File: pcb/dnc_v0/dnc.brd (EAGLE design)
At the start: 100 x 80 mm, 69 parts, among them IC1 74HC595D, IC2 74HC595D, Q1 200mA/50V, Q2 TSM2306CX, Q3 TSM2306CX, Q4 TSM2306CX, Q5 TSM2306CX, Q6 200mA/50V, Q7 TSM2306CX, Q8 TSM2306CX

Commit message: First try of routing, no analog atmega ?
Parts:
- removed IC1, IC2: 74HC595D, 74xx-eu:SO16
- removed JP1, JP10, JP11, JP9: M025MM, SparkFun-Connectors:SCREWTERMINAL-5MM-2
- removed JP12, JP20, JP21: M02LOCK_LONGPADS, SparkFun-Connectors:1X02_LOCK_LONGPADS
- removed JP2, JP3, JP4: (no value), SparkFun:1X03_LOCK_LONGPADS
- removed JP22: (no value), SparkFun:1X02_LONGPADS
- removed JP5, JP6, JP7, JP8: (no value), SparkFun:1X02_LOCK_LONGPADS
- removed Q1, Q6: 200mA/50V, SparkFun-DiscreteSemi:SOT23-3
- removed Q2, Q3, Q4: TSM2306CX, SparkFun-DiscreteSemi:SOT323
- removed SV1, SV2: (no value), con-lstb:MA08-2
- removed U$1, U$2, U$3, U$6, U$7, U$8: EXT-DNC, pierre_vv:EXTPINDNC
- added 3.3/5: (no value), SparkFun:1X02_LONGPADS
- added A+_UART, IN1, IN2, IN3, IN4: (no value), SparkFun:1X02_LOCK_LONGPADS
- added A_IN1, A_IN2, A_IN3: (no value), SparkFun:1X03_LOCK_LONGPADS
- added EXT1, EXT2, EXT3, EXT4, EXT5, EXT6: EXT-DNC, pierre_vv:EXTPINDNC
- added JP_OUT1, JP_OUT2, JP_OUT3: M02LOCK_LONGPADS, SparkFun-Connectors:1X02_LOCK_LONGPADS
- added MOS_BAT, MOS_TEMP: 200mA/50V, SparkFun-DiscreteSemi:SOT23-3
- added MOS_PWR1, MOS_PWR2, MOS_PWR3: TSM2306CX, SparkFun-DiscreteSemi:SOT323
- added PWR_OUT1, PWR_OUT2, PWR_OUT3, RAW_IN: M025MM, SparkFun-Connectors:SCREWTERMINAL-5MM-2
- added REG1, REG2: 74HC595D, 74xx-eu:SO16
- added TITREUR1, TITREUR2: (no value), con-lstb:MA08-2
- moved JP14 243.8 mm to (97.8, 22.9)
- moved JP13 242.6 mm to (101.6, 25.4)
- moved Q8 205.7 mm to (83.8, 52.1)
- moved Q7 194.1 mm to (83.8, 69.8)
- moved Q5 192.8 mm to (83.8, 61.0)
- moved C2 190.4 mm to (59.7, 48.3), turned to 270 degrees
- moved RIN4 185.1 mm to (45.7, 8.89)
- moved RIN7 184.6 mm to (81.3, 12.1)
- moved RIN3 178.4 mm to (39.4, 8.89), turned to 180 degrees
- moved RIN2 172.0 mm to (33.0, 8.89)
- moved RIN6 171.6 mm to (82.5, 27.9)
- moved RIN10 170.5 mm to (82.5, 48.3)
- moved JP19 169.1 mm to (97.8, 19.1)
- moved RIN1 165.2 mm to (25.4, 8.89), turned to 180 degrees
- moved RIN5 161.0 mm to (82.5, 39.4)
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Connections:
- removed net 3.3: U$1.3.3, U$2.3.3, U$3.3.3, U$6.3.3, U$7.3.3, U$8.3.3
- removed net N$31: U$4.8
- removed net N$32: U$4.10
- removed net N$33: U$4.12
- removed net N$34: U$4.16
- new net RXA+: A+_UART.2, U$4.10
- new net TXA+: A+_UART.1, U$4.8
- net +3V3: now also 3.3/5.1, A_IN1.2, A_IN2.2, A_IN3.2, EXT1.3.3V, EXT2.3.3V, EXT3.3.3V, EXT4.3.3V, EXT5.3.3V, EXT6.3.3V, IN1.1, IN2.1, IN3.1, IN4.1, REG1.10, REG2.10; no longer IC1.10, IC2.10, JP2.2, JP22.1, JP3.2, JP4.2, JP5.1, JP6.1, JP7.1, JP8.1
- net +5V: now also 3.3/5.2, EXT1.5V, EXT2.5V, EXT3.5V, EXT4.5V, EXT5.5V, EXT6.5V, TITREUR1.12, TITREUR1.14, TITREUR1.16, TITREUR2.12, TITREUR2.14, TITREUR2.16; no longer JP22.2, Q2.3, Q3.3, Q4.3, SV1.12, SV1.14, SV1.16, SV2.12, SV2.14, SV2.16
- net /CS_EXT_1: now also EXT1./RESET; no longer U$3./RESET
- net /CS_EXT_2: now also EXT2./RESET; no longer U$1./RESET
- net /CS_EXT_3: now also EXT3./RESET; no longer U$2./RESET
- net /CS_EXT_4: now also EXT4./RESET; no longer U$6./RESET
- net /CS_EXT_5: now also EXT5./RESET; no longer U$7./RESET
- net /CS_EXT_6: now also EXT6./RESET; no longer U$8./RESET
- net ACTIVE_ANALOG_RAW: now also MOS_BAT.1; no longer Q1.1
- net ACTIVE_ANALOG_TEMP: now also MOS_TEMP.1; no longer Q6.1
- net ACTIVE_OUT_POWER_1: now also MOS_PWR1.1; no longer Q3.1, U$4.36
- net ACTIVE_OUT_POWER_2: now also MOS_PWR2.1; no longer Q2.1, U$4.38
- net ACTIVE_OUT_POWER_3: now also MOS_PWR3.1; no longer Q4.1, U$4.40
- net ANALOG_IN_1: now also A_IN1.3; no longer JP2.3
- net ANALOG_IN_2: now also A_IN2.3; no longer JP3.3
- net ANALOG_IN_3: now also A_IN3.3; no longer JP4.3
- net ANALOG_RAW: now also MOS_BAT.2; no longer Q1.2
- net ANALOG_TEMP: now also MOS_TEMP.2; no longer Q6.2
- net CODE: now also EXT1.RETOURANALOG, EXT2.RETOURANALOG, EXT3.RETOURANALOG, EXT4.RETOURANALOG, EXT5.RETOURANALOG, EXT6.RETOURANALOG; no longer U$1.RETOURANALOG, U$2.RETOURANALOG, U$3.RETOURANALOG, U$6.RETOURANALOG, U$7.RETOURANALOG, U$8.RETOURANALOG
- net GND: now also A_IN1.1, A_IN2.1, A_IN3.1, EXT1.1_GND, EXT2.1_GND, EXT3.1_GND, EXT4.1_GND, EXT5.1_GND, EXT6.1_GND, JP_OUT1.2, JP_OUT2.2, JP_OUT3.2, PWR_OUT1.2, PWR_OUT2.2, PWR_OUT3.2, RAW_IN.2, REG1.13, REG1.8, REG2.13, REG2.8, TITREUR1.11, TITREUR1.13, TITREUR1.15, TITREUR1.8, TITREUR2.11, TITREUR2.13, TITREUR2.15, TITREUR2.8; no longer IC1.13, IC1.8, IC2.13, IC2.8, JP1.2, JP10.2, JP11.2, JP12.2, JP2.1, JP20.2, JP21.2, JP3.1, JP4.1, JP9.2, SV1.11, SV1.13, SV1.15, SV1.8, SV2.11, SV2.13, SV2.15, SV2.8, U$1.1_GND, U$2.1_GND, U$3.1_GND, U$6.1_GND, U$7.1_GND, U$8.1_GND
- net IN_1: now also IN1.2; no longer JP5.2
- net IN_2: now also IN2.2; no longer JP6.2
- net IN_3: now also IN3.2; no longer JP7.2
- net IN_4: now also IN4.2; no longer JP8.2
- net MISO: now also EXT1.MISO, EXT2.MISO, EXT3.MISO, EXT4.MISO, EXT5.MISO, EXT6.MISO; no longer U$1.MISO, U$2.MISO, U$3.MISO, U$6.MISO, U$7.MISO, U$8.MISO
- net MOSI: now also EXT1.MOSI, EXT2.MOSI, EXT3.MOSI, EXT4.MOSI, EXT5.MOSI, EXT6.MOSI; no longer U$1.MOSI, U$2.MOSI, U$3.MOSI, U$6.MOSI, U$7.MOSI, U$8.MOSI
- net N$10: now also EXT6.FREE; no longer U$8.FREE
- net N$11: now also MOS_TEMP.3; no longer Q6.3
- net N$12: now also RAW_IN.1; no longer JP1.1
- net N$21: now also EXT1.FREE; no longer U$3.FREE
- net N$3: now also MOS_BAT.3; no longer Q1.3
- net N$4: now also EXT2.FREE; no longer U$1.FREE
- net N$5: now also EXT3.FREE; no longer U$2.FREE
- net N$7: now also REG1.9, REG2.14; no longer IC1.9, IC2.14
- net N$8: now also EXT4.FREE; no longer U$6.FREE
- net N$9: now also EXT5.FREE; no longer U$7.FREE
- net OUT_1: now also JP_OUT1.1; no longer JP12.1
- net OUT_2: now also JP_OUT2.1; no longer JP20.1
- net OUT_3: now also JP_OUT3.1; no longer JP21.1
- net OUT_POWER_1: now also MOS_PWR1.2, PWR_OUT1.1; no longer JP9.1, Q3.2
- net OUT_POWER_2: now also MOS_PWR2.2, PWR_OUT2.1; no longer JP10.1, Q2.2
- net OUT_POWER_3: now also MOS_PWR3.2, PWR_OUT3.1; no longer JP11.1, Q4.2
- net RAW: now also EXT1.RAW, EXT2.RAW, EXT3.RAW, EXT4.RAW, EXT5.RAW, EXT6.RAW, MOS_PWR1.3, MOS_PWR2.3, MOS_PWR3.3; no longer U$1.RAW, U$2.RAW, U$3.RAW, U$6.RAW, U$7.RAW, U$8.RAW
- net RD: now also TITREUR1.6, TITREUR2.6; no longer SV1.6, SV2.6
- net REG_RCK: now also REG1.12, REG2.12; no longer IC1.12, IC2.12
- net REG_SCK: now also REG1.11, REG2.11; no longer IC1.11, IC2.11
- net REG_VAL: now also REG1.14; no longer IC1.14
- net RST1: now also REG1.15, TITREUR1.1; no longer IC1.15, SV1.1
- net RST10: now also REG2.1; no longer IC2.1
- net RST11: now also REG2.2; no longer IC2.2
- net RST12: now also REG2.3; no longer IC2.3
- net RST13: now also REG2.4; no longer IC2.4
- net RST14: now also REG2.5; no longer IC2.5
- net RST15: now also REG2.6; no longer IC2.6
- net RST16: now also REG2.7; no longer IC2.7
- net RST2: now also REG1.1, TITREUR1.2; no longer IC1.1, SV1.2
- net RST3: now also REG1.2, TITREUR1.3; no longer IC1.2, SV1.3
- net RST4: now also REG1.3, TITREUR1.4; no longer IC1.3, SV1.4
- net RST5: now also REG1.4, TITREUR2.1; no longer IC1.4, SV2.1
- net RST6: now also REG1.5, TITREUR2.2; no longer IC1.5, SV2.2
- net RST7: now also REG1.6, TITREUR2.3; no longer IC1.6, SV2.3
- net RST8: now also REG1.7, TITREUR2.4; no longer IC1.7, SV2.4
- net RST9: now also REG2.15; no longer IC2.15
- net SCK: now also EXT1.SCK, EXT2.SCK, EXT3.SCK, EXT4.SCK, EXT5.SCK, EXT6.SCK; no longer U$1.SCK, U$2.SCK, U$3.SCK, U$6.SCK, U$7.SCK, U$8.SCK
- net SYNC: now also TITREUR1.10, TITREUR2.10; no longer SV1.10, SV2.10
- net TIT_DATA: now also TITREUR1.7, TITREUR2.7; no longer SV1.7, SV2.7
- net TIT_OSC: now also TITREUR1.9, TITREUR2.9; no longer SV1.9, SV2.9
- net VCC: now also REG1.16, REG2.16; no longer IC1.16, IC2.16, U$1.VCC, U$2.VCC, U$3.VCC, U$6.VCC, U$7.VCC, U$8.VCC
- net WR: now also TITREUR1.5, TITREUR2.5; no longer SV1.5, SV2.5
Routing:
- net GND: track 0.00 -> 640.8 mm, vias 0 -> 1
- net +3V3: track 0.00 -> 407.1 mm, vias 0 -> 3
- net +5V: track 0.00 -> 264.9 mm, vias 0 -> 6
- net RESET: track 0.00 -> 236.3 mm, vias 0 -> 2
- net RAW: track 0.00 -> 221.1 mm, vias 0 -> 5
- net ACTIVE_OUT_3: track 0.00 -> 163.4 mm
- net MOSI: track 0.00 -> 152.7 mm, vias 0 -> 1
- net DTR: track 0.00 -> 144.5 mm, vias 0 -> 3
- net SCK: track 0.00 -> 126.2 mm, vias 0 -> 1
- net MISO: track 0.00 -> 123.2 mm
- net CODE: track 0.00 -> 122.9 mm, vias 0 -> 1
- net ACTIVE_OUT_2: track 0.00 -> 120.9 mm, vias 0 -> 4
- net IN_1: track 0.00 -> 68.7 mm, vias 0 -> 1
- net ACTIVE_OUT_1: track 0.00 -> 68.4 mm, vias 0 -> 1
- net IN_2: track 0.00 -> 58.7 mm, vias 0 -> 1
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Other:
- board outline removed

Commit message: Add a small link
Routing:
- net ACTIVE_OUT_POWER_2: track 2.98 -> 28.4 mm, vias 0 -> 2
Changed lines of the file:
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@@
 <wire x1="83.4" y1="27.94" x2="83.4" y2="30.595" width="0.254" layer="1"/>
 <wire x1="83.4" y1="30.595" x2="83.17" y2="30.825" width="0.254" layer="1"/>
-<wire x1="66.8274" y1="35.82" x2="83.17" y2="30.825" width="0" layer="19" extent="1-1"/>
+<wire x1="66.8274" y1="35.82" x2="68.955" y2="35.82" width="0.254" layer="1"/>
+<wire x1="68.955" y1="35.82" x2="69.85" y2="34.925" width="0.254" layer="1"/>
+<wire x1="69.85" y1="34.925" x2="73.025" y2="34.925" width="0.254" layer="1"/>
+<wire x1="73.025" y1="34.925" x2="74.93" y2="36.83" width="0.254" layer="1"/>
+<wire x1="74.93" y1="36.83" x2="79.375" y2="36.83" width="0.254" layer="1"/>
+<wire x1="83.17" y1="30.825" x2="83.17" y2="31.765" width="0.254" layer="1"/>
+<wire x1="83.17" y1="31.765" x2="81.915" y2="33.02" width="0.254" layer="1"/>
+<wire x1="81.915" y1="33.02" x2="81.915" y2="34.925" width="0.254" layer="1"/>
+<wire x1="81.915" y1="34.925" x2="83.82" y2="36.83" width="0.254" layer="1"/>
+<via x="79.375" y="36.83" extent="1-16" drill="0.6"/>
+<via x="83.82" y="36.83" extent="1-16" drill="0.6"/>
+<wire x1="79.375" y1="36.83" x2="83.82" y2="36.83" width="0.254" layer="16"/>
 </signal>
 <signal name="OUT_POWER_2">

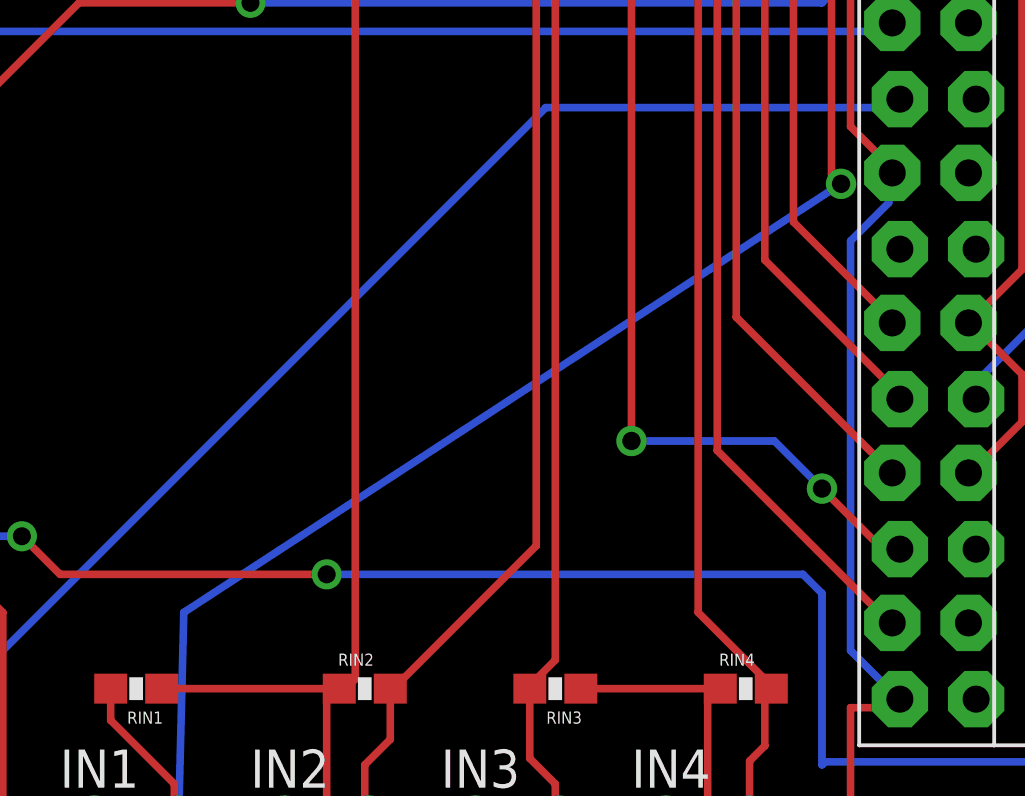
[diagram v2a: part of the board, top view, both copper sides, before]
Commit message: End (100%) first try, but no analog !
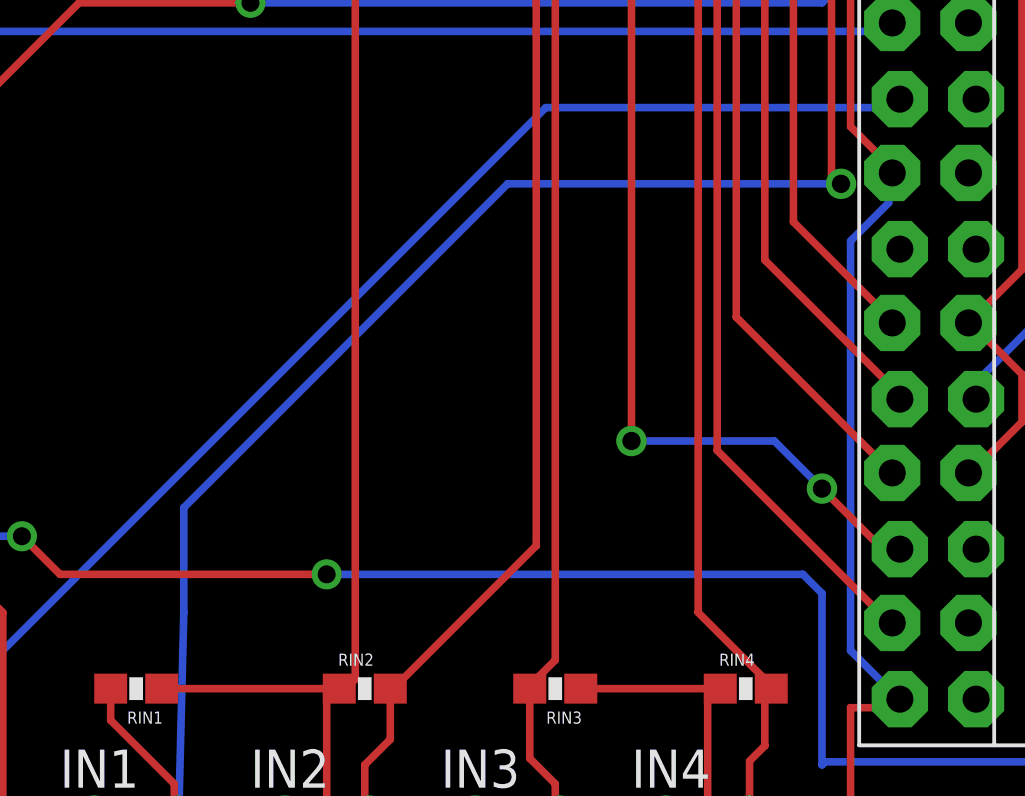
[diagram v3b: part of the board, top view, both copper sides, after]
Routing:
- net IN_1: track 68.7 -> 72.4 mm
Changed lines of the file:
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@@
 <wire x1="48.5775" y1="26.035" x2="48.5775" y2="51.1175" width="0.254" layer="1"/>
 <wire x1="48.895" y1="25.7175" x2="48.5775" y2="26.035" width="0.254" layer="1"/>
-<wire x1="26.9875" y1="11.43" x2="48.895" y2="25.7175" width="0.254" layer="16"/>
 <wire x1="50.8" y1="53.34" x2="50.857" y2="53.54" width="0.254" layer="1"/>
 <wire x1="26.9875" y1="11.43" x2="26.797" y2="3.81" width="0.254" layer="16"/>
 <via x="48.895" y="25.7175" extent="1-16" drill="0.6096"/>
+<wire x1="26.9875" y1="11.43" x2="26.9875" y2="14.9225" width="0.254" layer="16"/>
+<wire x1="26.9875" y1="14.9225" x2="37.7825" y2="25.7175" width="0.254" layer="16"/>
+<wire x1="37.7825" y1="25.7175" x2="48.895" y2="25.7175" width="0.254" layer="16"/>
 </signal>
 <signal name="IN_2">

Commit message: New brd far better, but not finished
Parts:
- removed C1, C16, C7: 0.1uF, rcl:C0805
- removed R1, R5, RIN5, RIN6, RIN7: 100k, SparkFun-Passives:0603-RES
- removed R2: 10k, SparkFun-Passives:0603-RES
- removed R26: 10K, rcl:R0603
- removed R3: (no value), ptc-ntc:P679
- removed R4: (no value), SparkFun-Passives:0603-RES
- removed R8: 100K, SparkFun-Passives:0603-RES
- added C3.3, CMHZ, CRST: 0.1uF, rcl:C0805
- added RBAT0: 100K, SparkFun-Passives:0603-RES
- added RBAT1, ROUT1, ROUT2, ROUT3, RTEMP0: 100k, SparkFun-Passives:0603-RES
- added RBAT2: 10k, SparkFun-Passives:0603-RES
- added RRST: 10K, rcl:R0603
- added RTEMP1: (no value), ptc-ntc:P679
- added RTEMP2: (no value), SparkFun-Passives:0603-RES
- moved JP19 105.9 mm to (1.52, 63.1)
- moved JP13 103.2 mm to (1.27, 1.27)
- moved JP_OUT2 65.5 mm to (66.2, 5.08), turned to 180 degrees
- moved JP_OUT1 61.9 mm to (61.1, 5.08), turned to 180 degrees
- moved Q7 58.4 mm to (66.2, 14.2)
- moved RIN9 57.7 mm to (65.5, 10.5), turned to 90 degrees
- moved Q5 51.9 mm to (61.3, 14.2)
- moved JP_OUT3 51.8 mm to (71.2, 5.08), turned to 180 degrees
- moved RIN8 50.7 mm to (60.6, 10.5), turned to 90 degrees
- moved 3.3/5 44.5 mm to (68.6, 40.6), turned to 90 degrees
- moved Q8 40.0 mm to (71.0, 14.2)
- moved RIN10 39.8 mm to (70.4, 10.4), turned to 90 degrees
- moved RCODE 37.1 mm to (65.0, 28.6), turned to 180 degrees
- moved A+_UART 37.0 mm to (58.4, 43.3), turned to 270 degrees
- moved F1 34.0 mm to (96.5, 56.3), turned to 270 degrees
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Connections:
- removed net N$15: U$4.7
- removed net N$18: U$4.15
- removed net N$23: U$4.27
- removed net N$35: U$4.18
- removed net N$36: U$4.22
- removed net N$37: U$4.24
- removed net N$38: U$4.26
- removed net N$39: U$4.28
- new net ANALOG_BAT: AT328.24
- net +3V3: now also C3.3.1, RRST.2, U$4.18; no longer C16.1, R26.2
- net +5V: now also RTEMP1.1; no longer R3.1
- net /CS_EXT_1: now also U$4.26
- net /CS_EXT_2: now also U$4.29
- net /CS_EXT_3: now also U$4.7
- net /CS_EXT_4: now also U$4.5
- net /CS_EXT_5: now also U$4.3
- net /CS_EXT_6: now also U$4.6
- net ACTIVE_ANALOG_RAW: now also RBAT0.2; no longer R8.2
- net ACTIVE_ANALOG_TEMP: now also RTEMP0.1; no longer R5.1
- net ACTIVE_OUT_1: now also U$4.36; no longer U$4.32
- net ACTIVE_OUT_2: now also U$4.38; no longer U$4.35
- net ACTIVE_OUT_3: now also U$4.40; no longer U$4.37
- net ACTIVE_OUT_POWER_1: now also ROUT1.2; no longer RIN5.2
- net ACTIVE_OUT_POWER_2: now also ROUT2.2; no longer RIN6.2
- net ACTIVE_OUT_POWER_3: now also ROUT3.2; no longer RIN7.2
- net ANALOG_IN_1: now also AT328.26
- net ANALOG_IN_2: now also AT328.27
- net ANALOG_IN_3: now also AT328.28
- net ANALOG_RAW: now also RBAT2.2; no longer R2.2
- net ANALOG_TEMP: now also AT328.25, RTEMP2.1; no longer R4.1
- net AREF: now also CMHZ.1; no longer C7.1
- net ATMEGA_CS: now also U$4.16; no longer U$4.6
- net CODE: now also AT328.23
- net DTR: now also CRST.1; no longer C1.1
- net GND: now also C3.3.2, CMHZ.2, RBAT0.1, RBAT2.1, ROUT1.1, ROUT2.1, ROUT3.1, RTEMP0.2, RTEMP2.2; no longer C16.2, C7.2, R2.1, R4.2, R5.2, R8.1, RIN5.1, RIN6.1, RIN7.1
- net IN_1: now also U$4.37; no longer U$4.3
- net IN_2: now also U$4.35; no longer U$4.5
- net IN_3: now also U$4.33; no longer U$4.11
- net IN_4: now also U$4.31; no longer U$4.13
- net N$11: now also RTEMP1.2; no longer R3.2
- net N$3: now also RBAT1.1; no longer R1.1
- net RAW: now also RBAT1.2; no longer R1.2
- net REG_RCK: now also U$4.11; no longer U$4.31
- net REG_SCK: now also U$4.15; no longer U$4.29
- net REG_VAL: now also U$4.13; no longer U$4.33
- net RESET: now also CRST.2, RRST.1; no longer C1.2, R26.1
- net RX-I: now also AT328.30
- net TX-O: now also AT328.31
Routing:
- net GND: track 640.8 -> 0.00 mm, vias 1 -> 0
- net ACTIVE_OUT_3: track 163.4 -> 2.04 mm
- net ACTIVE_OUT_2: track 120.9 -> 1.91 mm, vias 4 -> 0
- net RESET: track 236.3 -> 121.4 mm, vias 2 -> 1
- net DTR: track 144.5 -> 36.5 mm, vias 3 -> 0
- net MISO: track 123.2 -> 211.2 mm, vias 0 -> 6
- net SCK: track 126.2 -> 205.8 mm, vias 1 -> 6
- net /CS_EXT_1: track 0.00 -> 75.5 mm, vias 0 -> 2
- net /CS_EXT_6: track 0.00 -> 67.4 mm, vias 0 -> 2
- net ACTIVE_OUT_1: track 68.4 -> 1.95 mm, vias 1 -> 0
- net IN_1: track 72.4 -> 14.8 mm, vias 1 -> 0
- net /CS_EXT_3: track 0.00 -> 55.7 mm, vias 0 -> 2
- net /CS_EXT_5: track 0.00 -> 54.0 mm, vias 0 -> 2
- net REG_RCK: track 50.6 -> 0.00 mm, vias 2 -> 0
- net RST6: track 57.4 -> 10.2 mm
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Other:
- board outline added: 100 x 83.2 mm

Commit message: Little improvement
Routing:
- net +5V: track 251.8 -> 251.2 mm
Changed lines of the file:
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@@
 <contactref element="A+_UART" pad="1"/>
 <wire x1="53.397" y1="48.54" x2="53.397" y2="48.33" width="0.4064" layer="1"/>
-<wire x1="58.42" y1="43.434" x2="58.166" y2="43.434" width="0.4064" layer="1"/>
-<wire x1="58.166" y1="43.434" x2="55.88" y2="45.72" width="0.4064" layer="1"/>
-<wire x1="55.88" y1="45.72" x2="55.118" y2="45.72" width="0.4064" layer="1"/>
+<wire x1="58.42" y1="43.434" x2="57.15" y2="43.434" width="0.4064" layer="1"/>
+<wire x1="57.15" y1="43.434" x2="55.118" y2="45.72" width="0.4064" layer="1"/>
 <wire x1="55.118" y1="45.72" x2="55.118" y2="46.819" width="0.4064" layer="1"/>
 <wire x1="55.118" y1="46.819" x2="53.397" y2="48.54" width="0.4064" layer="1"/>
@@
 <wire x1="61.341" y1="15.149" x2="66.167" y2="15.149" width="1.016" layer="1"/>
 <wire x1="66.167" y1="15.149" x2="70.993" y2="15.149" width="1.016" layer="1"/>
-<wire x1="59.944" y1="45.593" x2="56.134" y2="47.244" width="1.016" layer="1"/>
-<wire x1="56.134" y1="47.244" x2="56.134" y2="50.803" width="1.016" layer="1"/>
+<wire x1="61.722" y1="46.355" x2="56.134" y2="46.482" width="1.016" layer="1"/>
+<wire x1="56.134" y1="46.482" x2="56.134" y2="50.803" width="1.016" layer="1"/>
 <wire x1="56.134" y1="50.803" x2="53.397" y2="53.54" width="1.016" layer="1"/>
 <wire x1="53.397" y1="53.54" x2="53.397" y2="55.823" width="1.016" layer="1"/>
@@
 <wire x1="27.94" y1="68.58" x2="30.48" y2="68.58" width="1.016" layer="1"/>
 <wire x1="25.4" y1="68.58" x2="25.4" y2="60.452" width="1.016" layer="1"/>
-<wire x1="68.58" y1="43.18" x2="61.722" y2="43.18" width="1.016" layer="1"/>
-<wire x1="61.722" y1="43.18" x2="59.944" y2="45.593" width="1.016" layer="1"/>
-<via x="56.134" y="47.244" extent="1-16" drill="0.6"/>
-<wire x1="56.134" y1="47.244" x2="56.134" y2="30.226" width="1.016" layer="16"/>
+<wire x1="68.58" y1="43.18" x2="66.294" y2="43.18" width="1.016" layer="1"/>
+<wire x1="66.294" y1="43.18" x2="61.722" y2="46.355" width="1.016" layer="1"/>
+<via x="56.134" y="46.482" extent="1-16" drill="0.6"/>
+<wire x1="56.134" y1="46.482" x2="56.134" y2="30.226" width="1.016" layer="16"/>
 <via x="56.134" y="30.226" extent="1-16" drill="0.6"/>
 <wire x1="56.134" y1="30.226" x2="56.134" y2="27.559" width="1.016" layer="1"/>

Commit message: Manual brd just before GND
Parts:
- moved REG2 5.18 mm to (41.9, 48.0), turned to 180 degrees
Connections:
- removed net RD: TITREUR1.6, TITREUR2.6
- removed net REG_SCK: REG1.11, REG2.11, U$4.15
- removed net REG_VAL: REG1.14, U$4.13
- removed net SYNC: TITREUR1.10, TITREUR2.10
- removed net TIT_DATA: TITREUR1.7, TITREUR2.7
- removed net TIT_OSC: TITREUR1.9, TITREUR2.9
- removed net WR: TITREUR1.5, TITREUR2.5
- net ACTIVE_OUT_POWER_1: now also AT328.32
- net MOSI: now also REG1.14, TITREUR1.7, TITREUR2.7
- net SCK: now also REG1.11, REG2.11, TITREUR1.5, TITREUR2.5
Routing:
- net MOSI: track 199.9 -> 281.4 mm, vias 5 -> 6
- net SCK: track 205.8 -> 281.9 mm, vias 6 -> 8
- net ACTIVE_OUT_POWER_3: track 8.25 -> 45.8 mm, vias 0 -> 2
- net ACTIVE_OUT_3: track 2.04 -> 33.8 mm
- net REG_RCK: track 0.00 -> 29.9 mm, vias 0 -> 1
- net ACTIVE_OUT_2: track 1.91 -> 29.6 mm
- net N$7: track 0.00 -> 22.8 mm
- net ACTIVE_OUT_POWER_2: track 14.2 -> 35.3 mm, vias 2 -> 4
- net +3V3: track 392.7 -> 409.7 mm, vias 7 -> 9
- net VCC: track 0.00 -> 16.3 mm
- net ACTIVE_OUT_POWER_1: track 21.6 -> 33.3 mm, vias 2 -> 3
- net ACTIVE_OUT_1: track 1.95 -> 11.3 mm
- net CODE: track 160.3 -> 162.3 mm

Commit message: Place labels
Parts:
- renumbered ISP1 to ISP, JP_OUT1 to OUT1, JP_OUT2 to OUT2, JP_OUT3 to OUT3, RTEMP1 to PTC
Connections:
- new net REG_CLR: REG1.10, REG2.10, U$4.13
- net +3V3: no longer REG1.10, REG2.10
- net /CS_EXT_1: now also U$4.32; no longer U$4.26
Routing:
- net REG_CLR: track 0.00 -> 38.5 mm, vias 0 -> 3
- net /CS_EXT_1: track 75.5 -> 68.4 mm
- net +3V3: track 409.7 -> 404.9 mm, vias 9 -> 7
- net RAW: track 255.4 -> 252.6 mm
- net CODE: track 162.3 -> 164.4 mm, vias 4 -> 3
- net SCK: track 281.9 -> 281.3 mm
